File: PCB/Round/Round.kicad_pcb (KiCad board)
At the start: 2 copper layers, 70 x 70 mm, 59 parts, among them J3 Conn, SW1 ESE13V01D, U1 PN532, U2 QR, Y1 27.12MHz

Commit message: PCB Update
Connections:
- A1 pad 0: (no net) -> unconnected-(A1-LOOP-Pad0)_7

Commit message: Tidy
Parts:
- removed U2: QR, RevK:QR-PN532

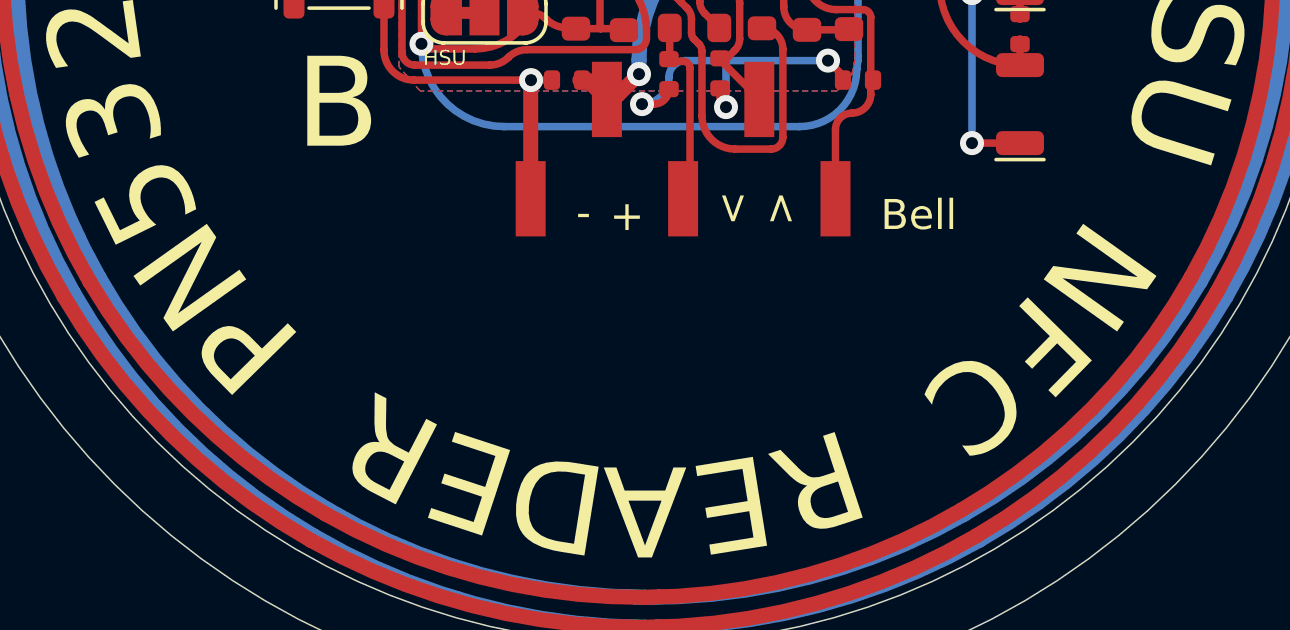
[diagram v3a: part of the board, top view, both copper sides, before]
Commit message: Re-do case
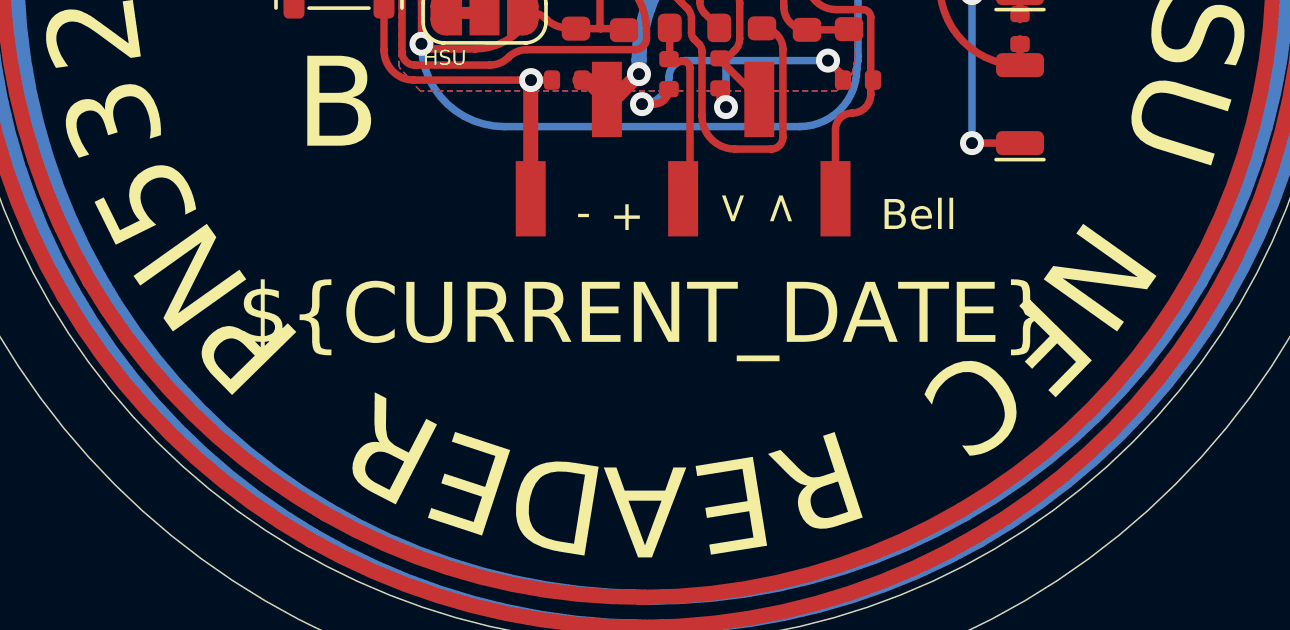
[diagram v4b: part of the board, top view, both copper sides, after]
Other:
- board text added: "${CURRENT_DATE}"

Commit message: Change part
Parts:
- moved D6 1.70 mm to (105.4, 104.1), turned to 90 degrees
- moved D10 0.14 mm to (97.3, 104.1), turned to -90 degrees
- moved D9 0.12 mm to (102.5, 104.1)
- moved D8 0.10 mm to (100.8, 104.1)
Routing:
- net Net-(J3-Pin_5): track 9.35 -> 11.4 mm
